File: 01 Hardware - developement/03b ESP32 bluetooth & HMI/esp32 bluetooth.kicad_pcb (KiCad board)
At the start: 2 copper layers, 152.4 x 142.2 mm, 127 parts, among them J1 I2C, J10 Conn_01x02_Pin, J11 Conn_01x02_Pin, J2 UART, J3 power supply, J4 Jtag, J5 I2S, J6 Backlight and leds, J7 to stepper motor, J8 Conn_01x01_Pin, J9 Conn_02x05_Odd_Even, Q1 BC817, Q2 BSS138, Q3 BSS138, Q4 BSS138, SW1 SW_Push_Dual, SW10 Strapping button, SW2 SW_Push_Dual, SW3 SW_Push_Dual, SW4 SW_Push_Dual, SW5 SW_Push_Dual, SW6 Rotary_Encoder_Switch, SW7 Rotary_Encoder_Switch, SW8 Strapping button, SW9 Strapping button, U1 DRV8825_STEPPER_MOTOR_DRIVER_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, U2 ESP32-DevKitC, U3 MCP23008

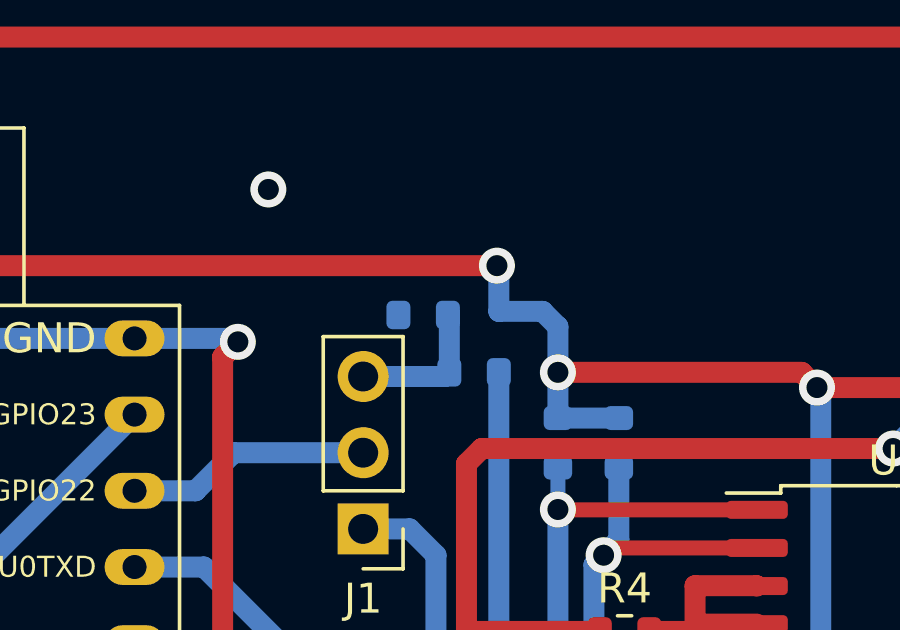
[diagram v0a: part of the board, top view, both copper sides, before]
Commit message: poprawka esp32 GPIO0 z pulldown do pullup
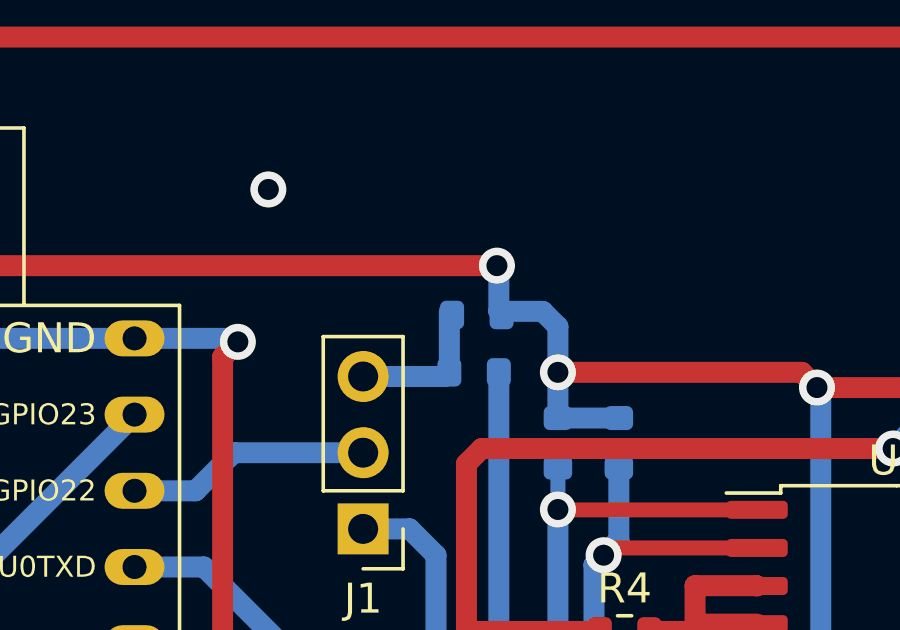
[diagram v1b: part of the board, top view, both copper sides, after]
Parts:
- moved R57 1.79 mm to (121.2, 80.4), turned to 0 degrees
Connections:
- R57 pad 2: GNDD -> +3V3
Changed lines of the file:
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@@
 	(footprint "Resistor_SMD:R_0603_1608Metric"
 		(layer "B.Cu")
-		(at 119.460595 80.384893 180)
+		(at 121.25 80.384893)
 		(descr "Resistor SMD 0603 (1608 Metric), square (rectangular) end terminal, IPC_7351 nominal, (Body size source: IPC-SM-782 page 72, https://www.pcb-3d.com/wordpress/wp-content/uploads/ipc-sm-782a_amendment_1_and_2.pdf), generated with kicad-footprint-generator")
 		(tags "resistor")
@@
 		)
 		(property "Datasheet" "~"
-			(at 0 0 180)
+			(at 0 0 0)
 			(layer "F.Fab")
 			(hide yes)
@@
 		)
 		(property "Description" ""
-			(at 0 0 180)
+			(at 0 0 0)
 			(layer "F.Fab")
 			(hide yes)
@@
 		(attr smd)
 		(fp_line
+			(start -0.237258 -0.5225)
+			(end 0.237258 -0.5225)
+			(stroke
+				(width 0.12)
+				(type solid)
+			)
+			(layer "B.SilkS")
+		)
+		(fp_line
 			(start -0.237258 0.5225)
 			(end 0.237258 0.5225)
@@
 		)
 		(fp_line
-			(start -0.237258 -0.5225)
-			(end 0.237258 -0.5225)
+			(start -1.48 -0.73)
+			(end -1.48 0.73)
 			(stroke
-				(width 0.12)
+				(width 0.05)
 				(type solid)
 			)
-			(layer "B.SilkS")
+			(layer "B.CrtYd")
 		)
 		(fp_line
-			(start 1.48 0.73)
-			(end 1.48 -0.73)
+			(start -1.48 0.73)
+			(end 1.48 0.73)
 			(stroke
 				(width 0.05)
@@
 		)
 		(fp_line
-			(start -1.48 0.73)
-			(end 1.48 0.73)
+			(start 1.48 0.73)
+			(end 1.48 -0.73)
 			(stroke
 				(width 0.05)
@@
 		)
 		(fp_line
-			(start -1.48 -0.73)
-			(end -1.48 0.73)
+			(start -0.8 -0.4125)
+			(end -0.8 0.4125)
 			(stroke
-				(width 0.05)
+				(width 0.1)
 				(type solid)
 			)
-			(layer "B.CrtYd")
+			(layer "B.Fab")
 		)
 		(fp_line
-			(start 0.8 0.4125)
-			(end 0.8 -0.4125)
+			(start -0.8 0.4125)
+			(end 0.8 0.4125)
 			(stroke
 				(width 0.1)
@@
 		)
 		(fp_line
-			(start -0.8 0.4125)
-			(end 0.8 0.4125)
-			(stroke
-				(width 0.1)
-				(type solid)
-			)
-			(layer "B.Fab")
-		)
-		(fp_line
-			(start -0.8 -0.4125)
-			(end -0.8 0.4125)
+			(start 0.8 0.4125)
+			(end 0.8 -0.4125)
 			(stroke
 				(width 0.1)
@@
 		)
 		(pad "1" smd roundrect
-			(at -0.825 0 180)
+			(at -0.825 0)
 			(size 0.8 0.95)
 			(layers "B.Cu" "B.Mask" "B.Paste")
@@
 		)
 		(pad "2" smd roundrect
-			(at 0.825 0 180)
+			(at 0.825 0)
 			(size 0.8 0.95)
 			(layers "B.Cu" "B.Mask" "B.Paste")
 			(roundrect_rratio 0.25)
-			(net 2 "GNDD")
+			(net 47 "+3V3")
 			(pintype "passive")
 		)
